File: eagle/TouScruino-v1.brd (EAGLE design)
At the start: 63.5 x 66 mm, 46 parts, among them J1 AVR_ISP, Q1 8MHz, Q2 MMBT2222, Q3 8MHz, U1 ATMEGA1284P, U3 ARDUINO_SHIELD, U4 MCP73831, U5 MIC5209-3.3YS, X1 USBSMD

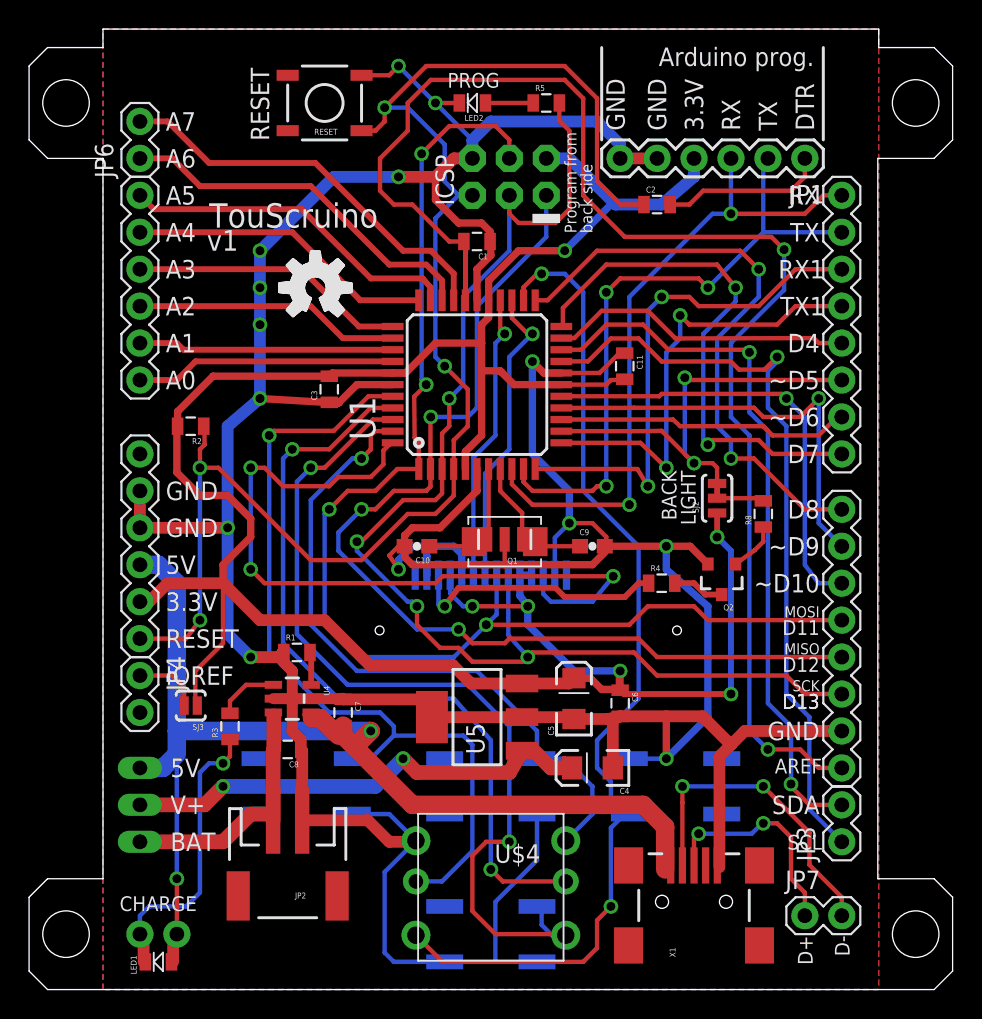
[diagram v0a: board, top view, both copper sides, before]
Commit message: 
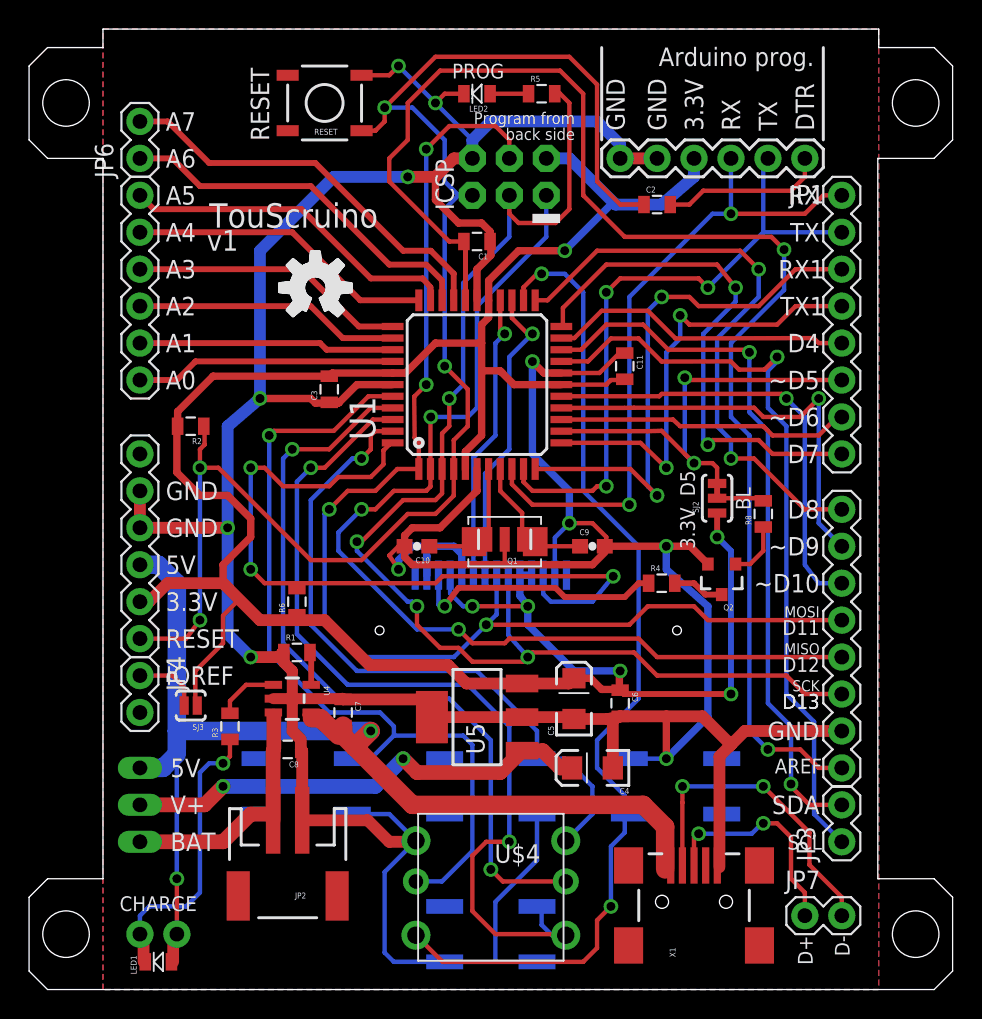
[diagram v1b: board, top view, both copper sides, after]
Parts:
- added R6: 10k, SparkFun:0805
- moved R5 0.71 mm to (35.2, 61.6)
- moved LED2 0.71 mm to (30.8, 61.6)
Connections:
- net 3.3V: now also R6.1
- net D18: now also R6.2
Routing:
- net D2/RX1: track 35.5 -> 37.1 mm
- net D13/SCK: track 88.7 -> 89.8 mm
- net RES: track 102.0 -> 102.7 mm
- net GND: track 315.6 -> 316.3 mm, vias 14 -> 11
- net N$5: track 3.28 -> 2.64 mm
- net AREF: track 100.0 -> 99.4 mm
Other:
- board text added: "BL"
- board text added: "D5"
- board text removed: "BACK LIGHT"
